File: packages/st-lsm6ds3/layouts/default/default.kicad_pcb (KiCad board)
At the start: 2 copper layers, 7 parts

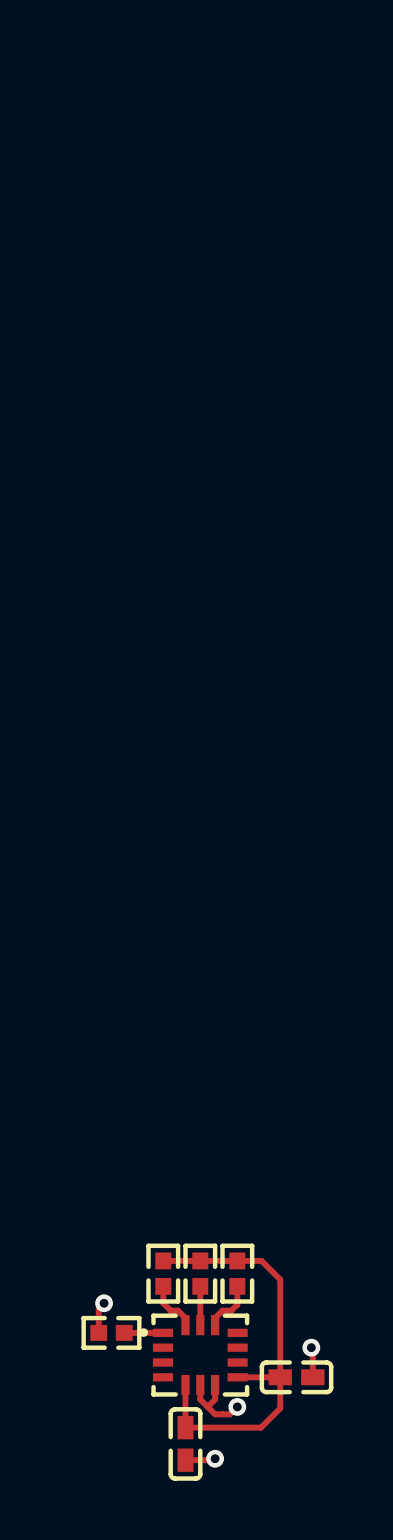
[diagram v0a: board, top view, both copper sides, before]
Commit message: fix leds, orphaning old package name with package in title
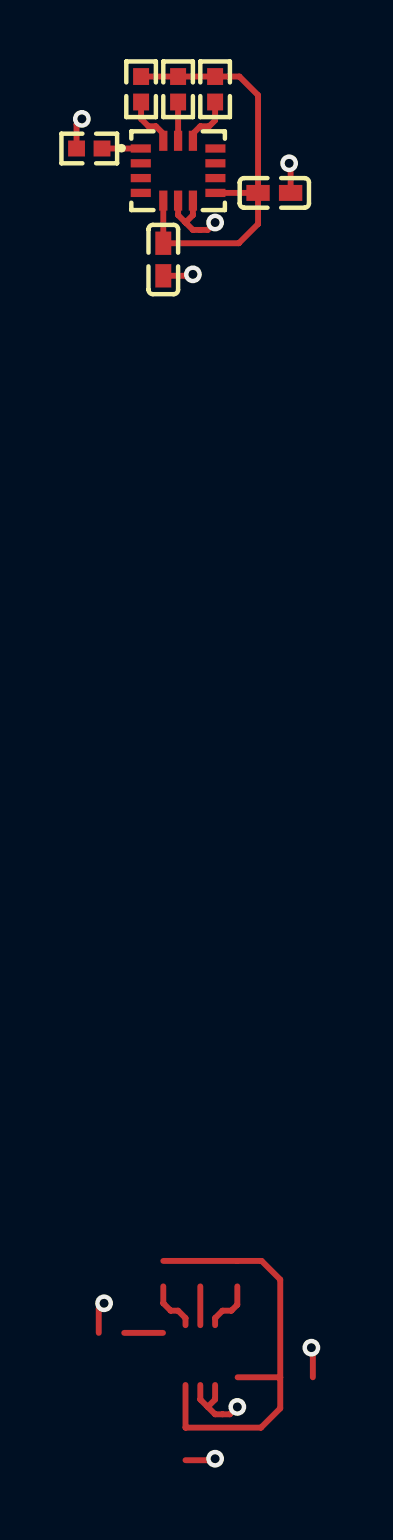
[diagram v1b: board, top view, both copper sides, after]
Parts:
- moved C1 40.0 mm to (-0.50, -37.0)
- moved C2 40.0 mm to (3.25, -39.2)
- moved R1 40.0 mm to (1.25, -42.8)
- moved R2 40.0 mm to (-3.00, -40.8)
- moved R3 40.0 mm to (0.00, -42.8)
- moved R4 40.0 mm to (-1.25, -42.8)
- moved U1 40.0 mm to (0.00, -40.0)
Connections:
- net footprint-net-0 renamed accelerometer-net-0
- net footprint-net-1 renamed accelerometer-net-1
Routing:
- net (no net): track 0.00 -> 27.1 mm, vias 0 -> 4

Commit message: fixing up more thigns
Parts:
- R3, R4: value 10kΩ ±1% 62.5mW -> 4.7kΩ ±1% 62.5mW; footprint UNI_ROYAL_0402WGF1002TCE:R0402 -> UNI_ROYAL_0402WGF4701TCE:R0402
- moved R1 42.8 mm to (0.00, 0.00), turned to 0 degrees
- moved C1 27.0 mm to (0.00, -10.0), turned to 0 degrees
- moved C2 19.5 mm to (0.00, -20.0)
- moved R4 17.3 mm to (0.00, -60.0), turned to 0 degrees
- moved R2 11.2 mm to (0.00, -30.0)
- moved R3 7.25 mm to (0.00, -50.0), turned to 0 degrees
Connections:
- net accelerometer-net-0 renamed footprint-net-0
- net accelerometer-net-1 renamed footprint-net-1
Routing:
- net (no net): track 27.1 -> 54.2 mm, vias 4 -> 8
- net VCC: track 14.9 -> 0.00 mm
- net GND: track 6.01 -> 0.00 mm, vias 4 -> 0
- net CS: track 1.80 -> 0.00 mm
- net SDA: track 1.77 -> 0.00 mm
- net SCL: track 1.31 -> 0.00 mm
- net SDO_SA0: track 1.31 -> 0.00 mm

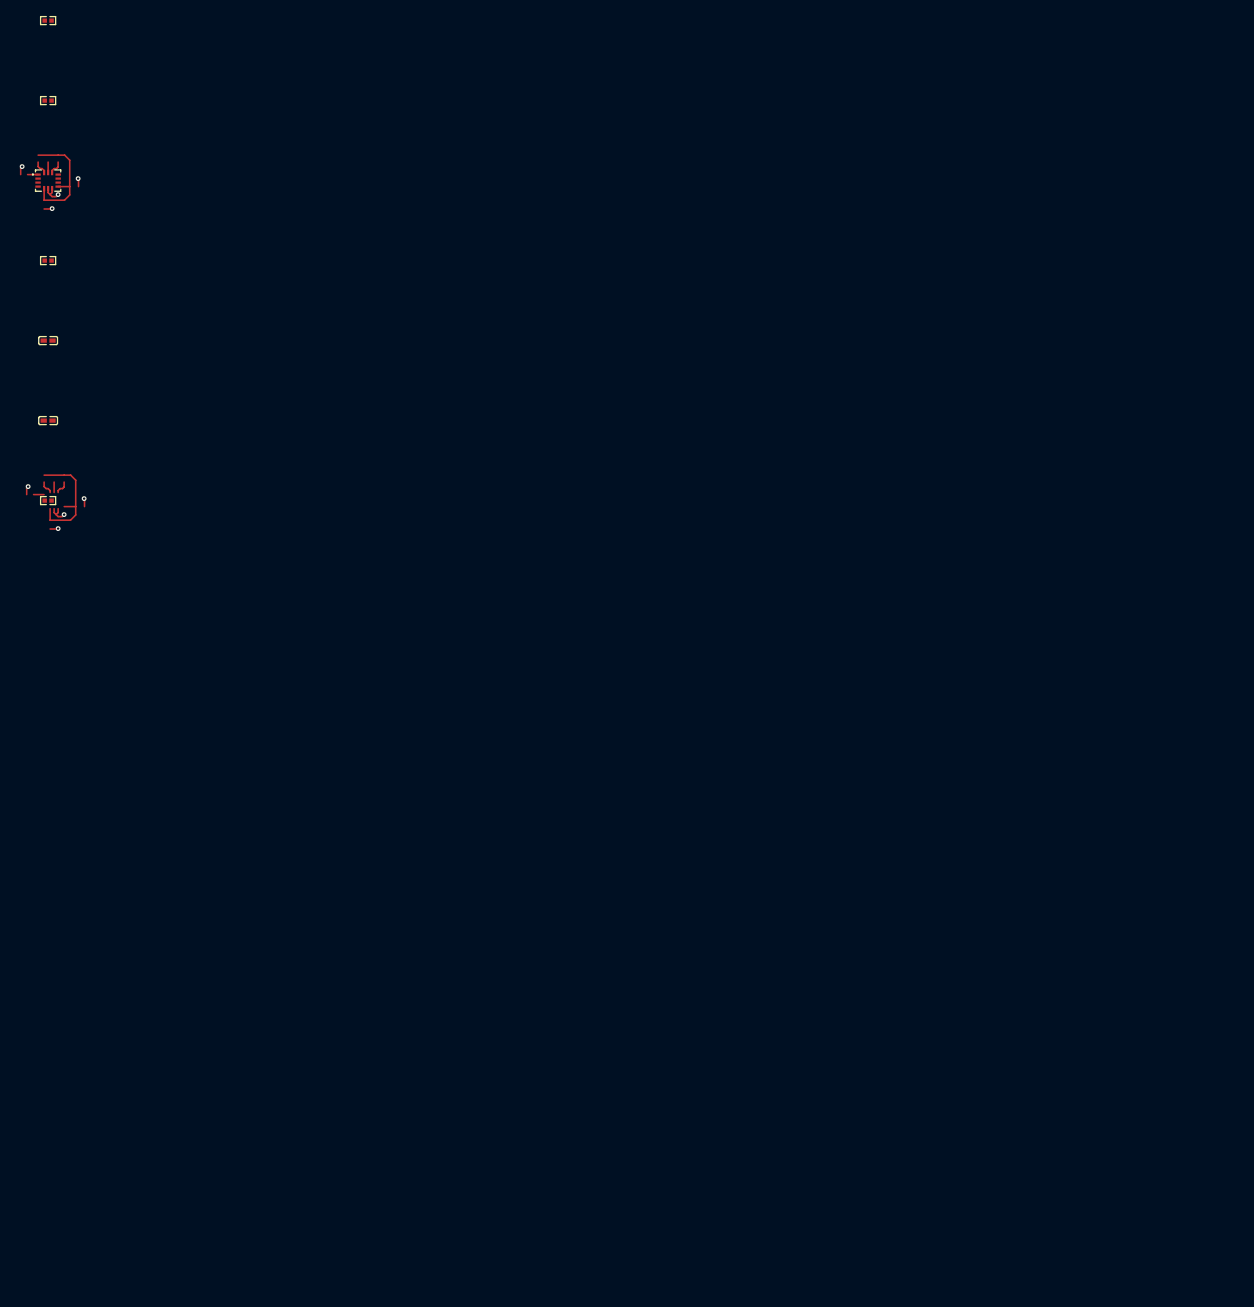
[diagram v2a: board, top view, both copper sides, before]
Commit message: deleting double package
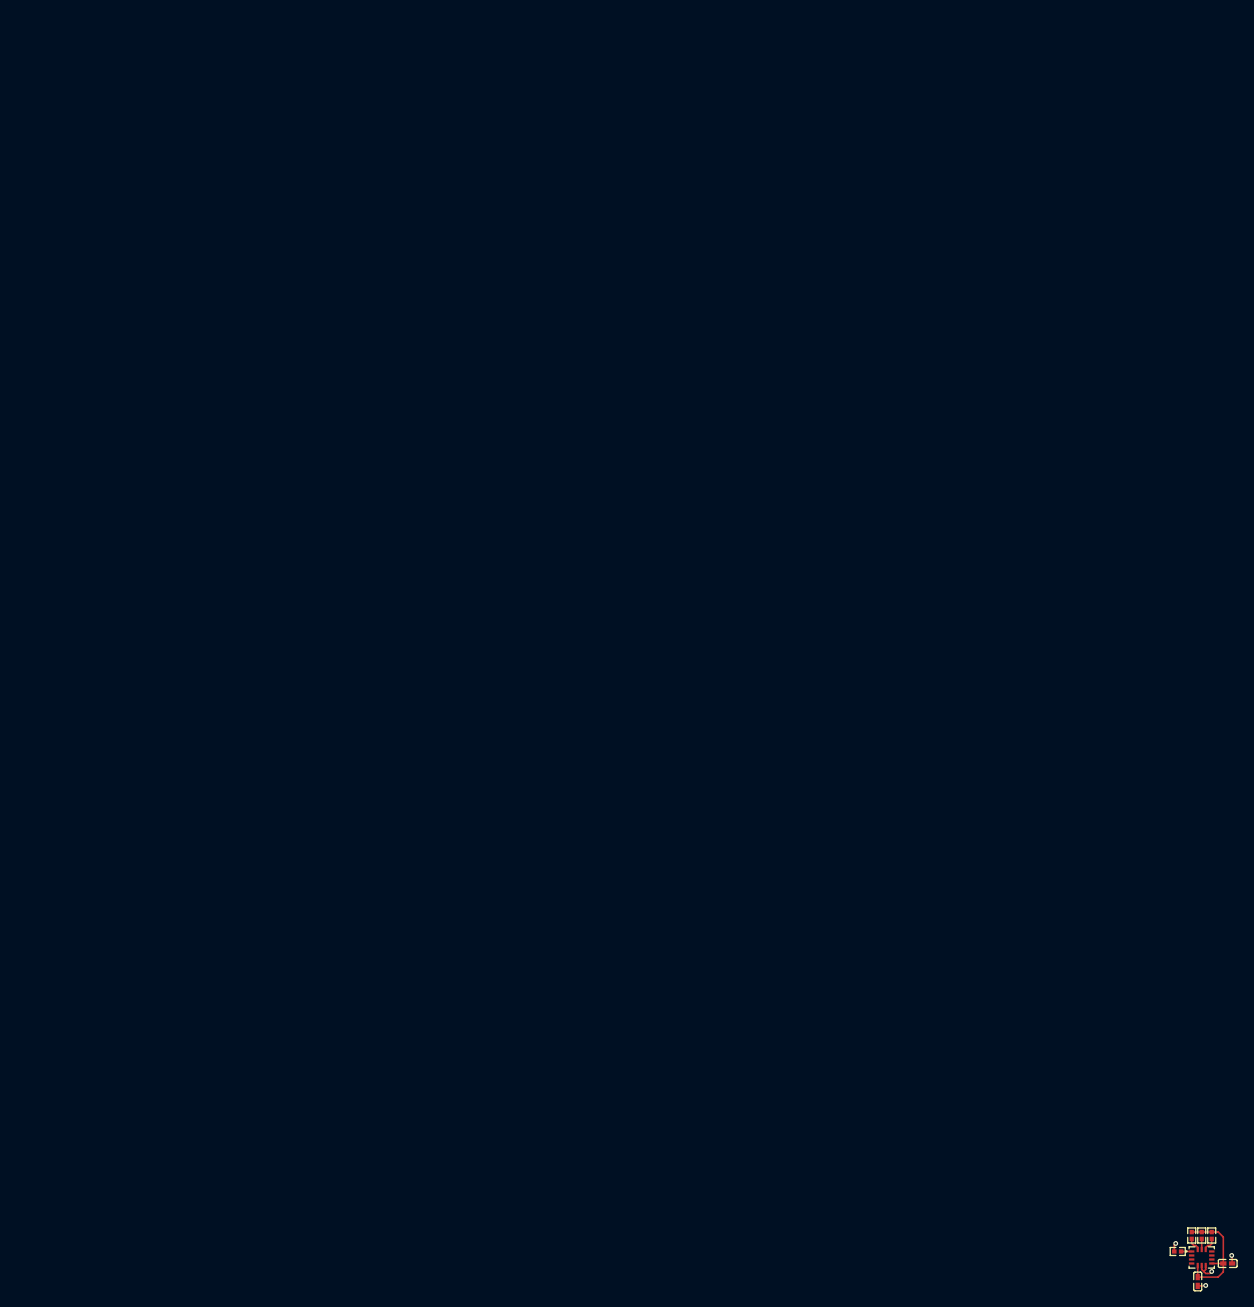
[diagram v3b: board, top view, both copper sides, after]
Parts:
- moved R4 208.6 mm to (142.9, 91.9), turned to 90 degrees
- moved R3 202.3 mm to (144.2, 91.9), turned to 90 degrees
- moved U1 197.3 mm to (144.2, 94.6)
- moved R2 187.8 mm to (141.2, 93.9)
- moved C2 185.7 mm to (143.7, 97.6), turned to -90 degrees
- moved C1 181.2 mm to (147.4, 95.4)
- moved R1 172.0 mm to (145.4, 91.9), turned to -90 degrees
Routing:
- net (no net): track 54.2 -> 0.00 mm, vias 8 -> 0
- net VCC: track 0.00 -> 14.9 mm
- net GND: track 0.00 -> 6.01 mm, vias 0 -> 4
- net CS: track 0.00 -> 1.80 mm
- net SDA: track 0.00 -> 1.77 mm
- net SDO_SA0: track 0.00 -> 1.31 mm
- net SCL: track 0.00 -> 1.31 mm
